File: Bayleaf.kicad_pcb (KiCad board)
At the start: 2 copper layers, 137 x 94 mm, 71 parts, among them J2 Conn_01x02_Socket, SW1 SW_SPDT, U1 Nice_Nano_V2

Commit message: images
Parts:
- moved H2 1.00 mm to (111.0, 3.00)
- moved H3 1.00 mm to (135.0, 3.00)
- moved H5 1.00 mm to (111.0, 91.0)
- moved H6 1.00 mm to (135.0, 91.0)
- moved H7 1.00 mm to (111.0, 47.0)
- moved J2 1.00 mm to (116.0, 86.0)
- moved U1 1.00 mm to (123.0, 17.8)
- moved SW1 0.97 mm to (123.0, 91.9)
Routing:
- net col-4L: track 130.8 -> 135.9 mm
- net col-5L: track 103.9 -> 106.7 mm
- net col-2L: track 166.6 -> 167.9 mm
- net col-1L: track 183.0 -> 184.3 mm
- net col-3L: track 171.5 -> 170.3 mm
- net row-4L: track 171.2 -> 172.3 mm
- net col-0L: track 234.6 -> 235.6 mm
- net row-3L: track 185.6 -> 186.2 mm
- net row-2L: track 202.1 -> 202.6 mm
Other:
- board size 137 x 94 mm -> 138 x 94 mm

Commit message: move sw
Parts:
- moved U1 0.91 mm to (123.0, 18.7)
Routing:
- net col-5L: track 106.7 -> 108.3 mm
- net row-4L: track 172.3 -> 171.3 mm
- net row-3L: track 186.2 -> 185.3 mm
- net RESET: track 77.6 -> 76.7 mm
- net RAW: track 94.8 -> 93.8 mm
- net row-2L: track 202.6 -> 201.8 mm
- net row-1L: track 223.4 -> 222.7 mm
- net col-0L: track 235.6 -> 236.1 mm
- net row-0L: track 240.9 -> 240.4 mm

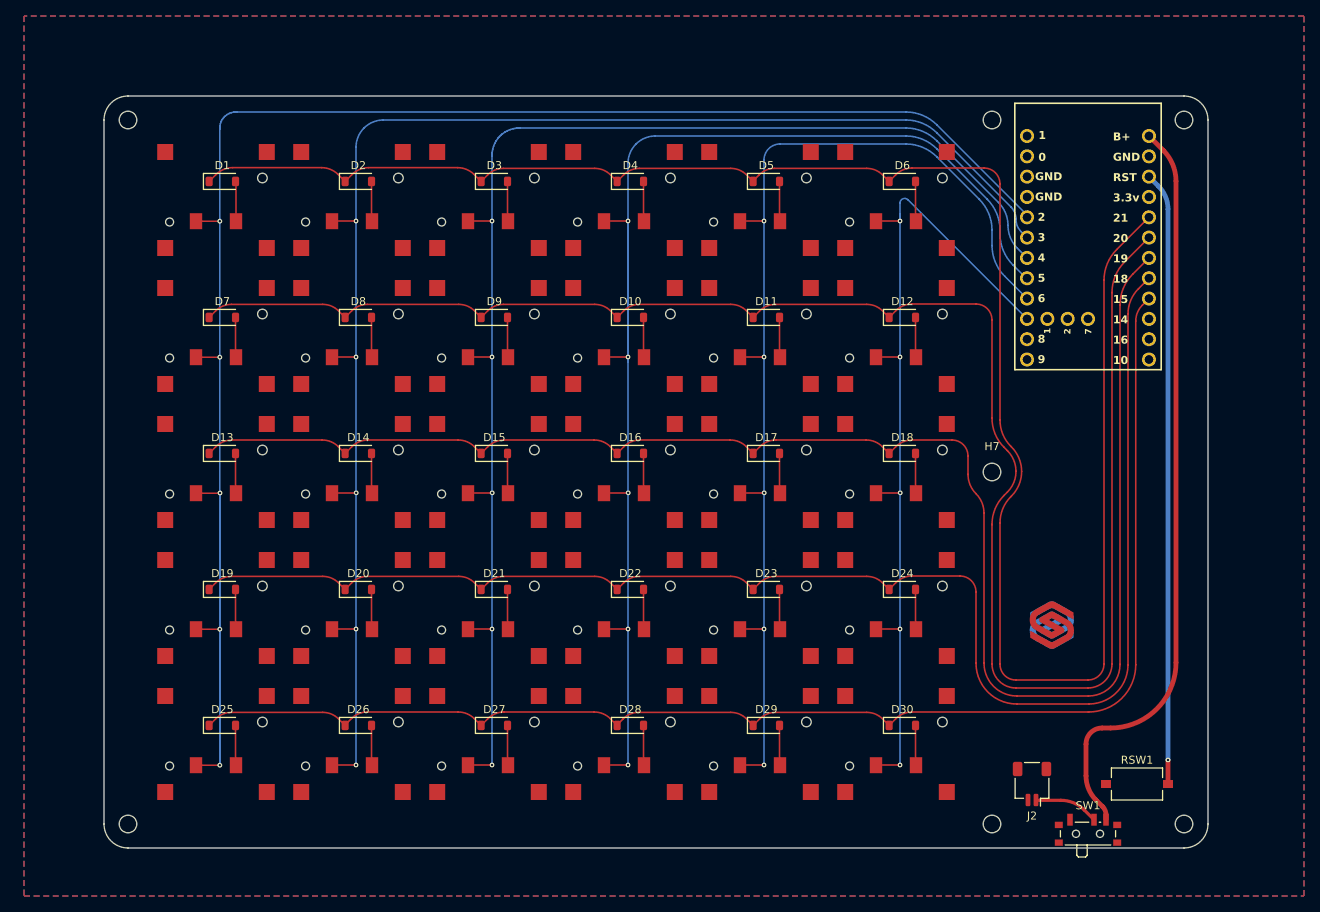
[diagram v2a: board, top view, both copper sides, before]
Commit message: Move components to fit under slope
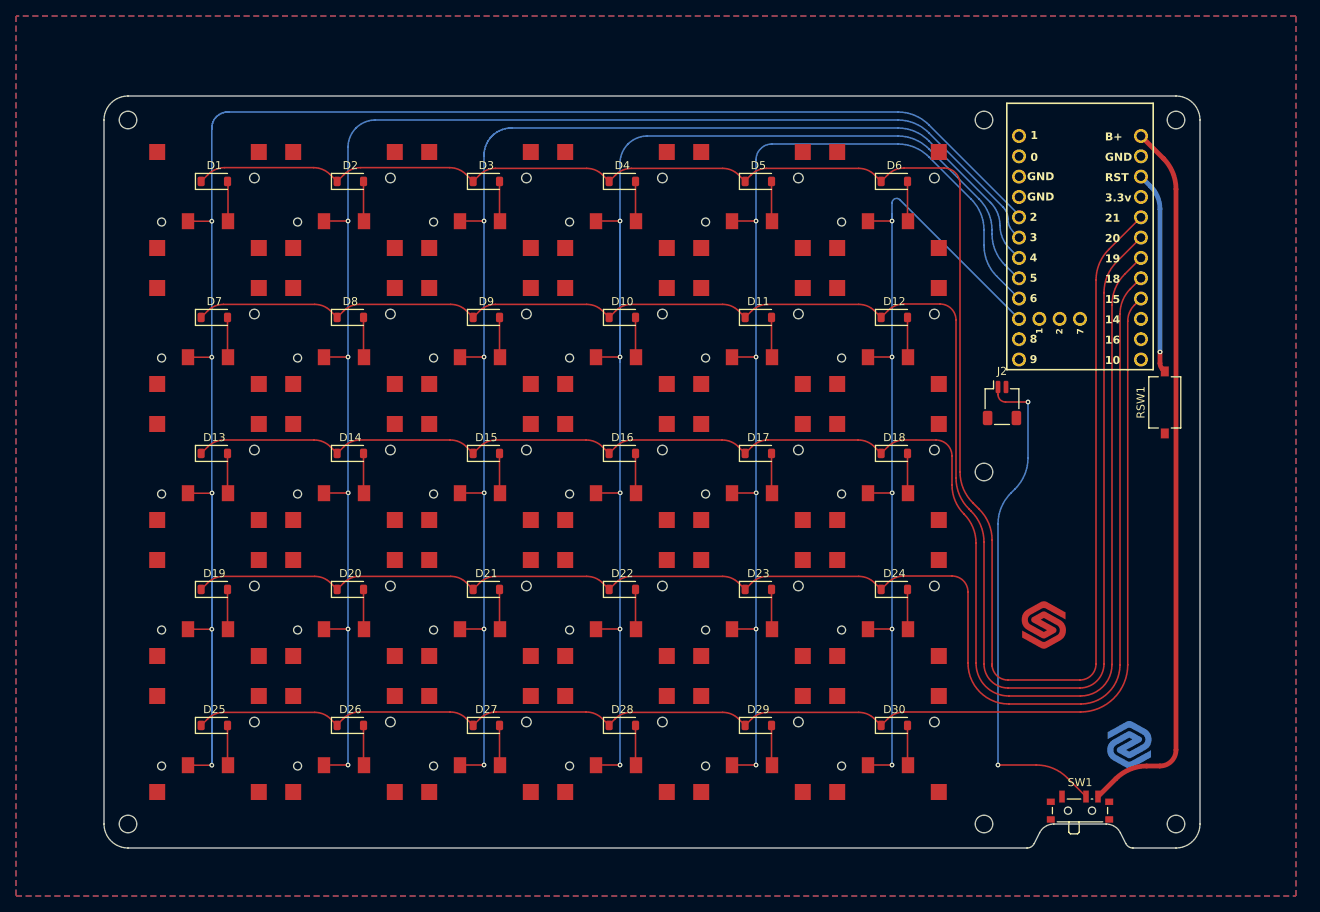
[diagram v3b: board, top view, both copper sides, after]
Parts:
- moved RSW1 47.8 mm to (132.6, 38.3), turned to 90 degrees
- moved J2 47.8 mm to (112.2, 38.4), turned to 0 degrees
- moved SW1 3.06 mm to (122.0, 89.0)
- moved D1 1.00 mm to (13.8, 10.7)
- moved D10 1.00 mm to (64.8, 27.7)
- moved D11 1.00 mm to (81.8, 27.7)
- moved D12 1.00 mm to (98.8, 27.7)
- moved D13 1.00 mm to (13.8, 44.7)
- moved D14 1.00 mm to (30.8, 44.7)
- moved D15 1.00 mm to (47.8, 44.7)
- moved D16 1.00 mm to (64.8, 44.7)
- moved D17 1.00 mm to (81.8, 44.7)
- moved D18 1.00 mm to (98.8, 44.7)
- moved D19 1.00 mm to (13.8, 61.7)
- moved D2 1.00 mm to (30.8, 10.7)
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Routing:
- net +BATT: track 8.07 -> 64.0 mm, vias 0 -> 2
- net RESET: track 76.7 -> 25.3 mm
- net row-1L: track 222.7 -> 218.5 mm
- net row-0L: track 240.4 -> 236.4 mm
- net RAW: track 93.8 -> 90.4 mm
- net row-2L: track 201.8 -> 201.0 mm
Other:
- board size 138 x 94 mm -> 137 x 94 mm

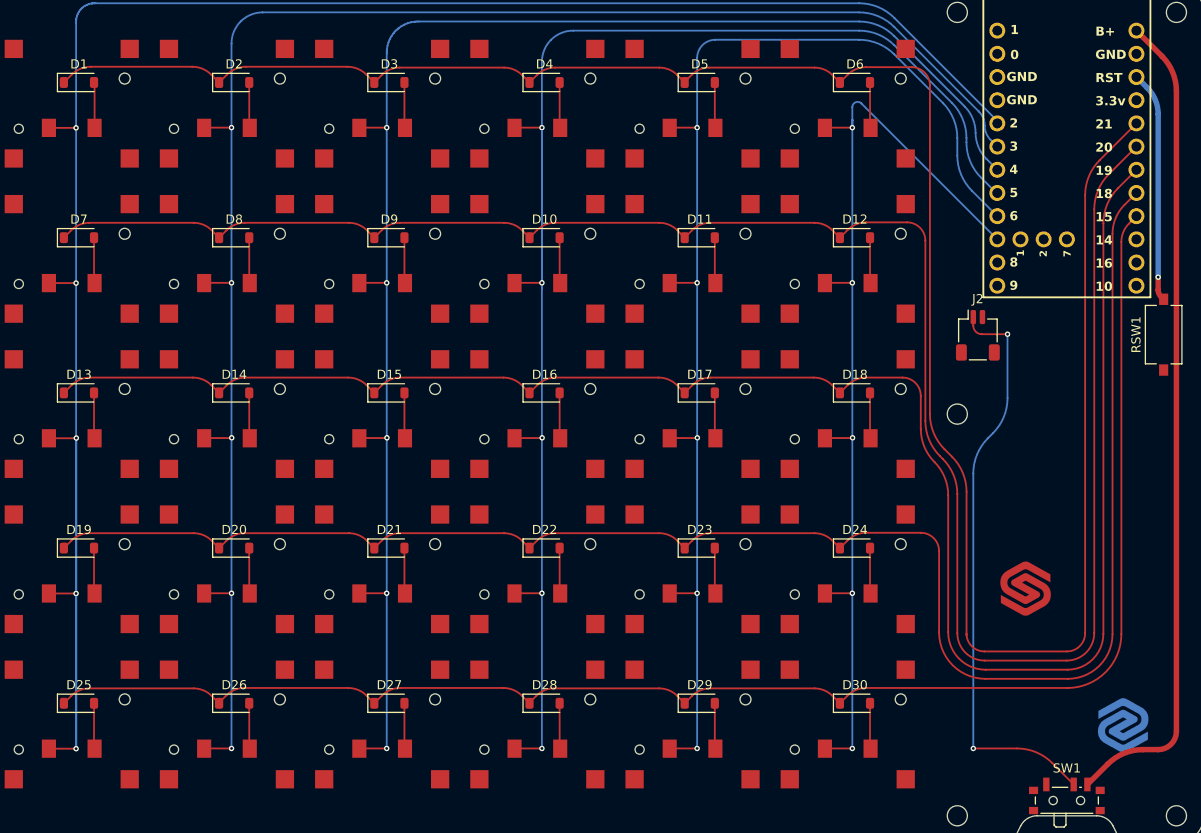
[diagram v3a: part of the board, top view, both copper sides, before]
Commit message: renamed schematic refs
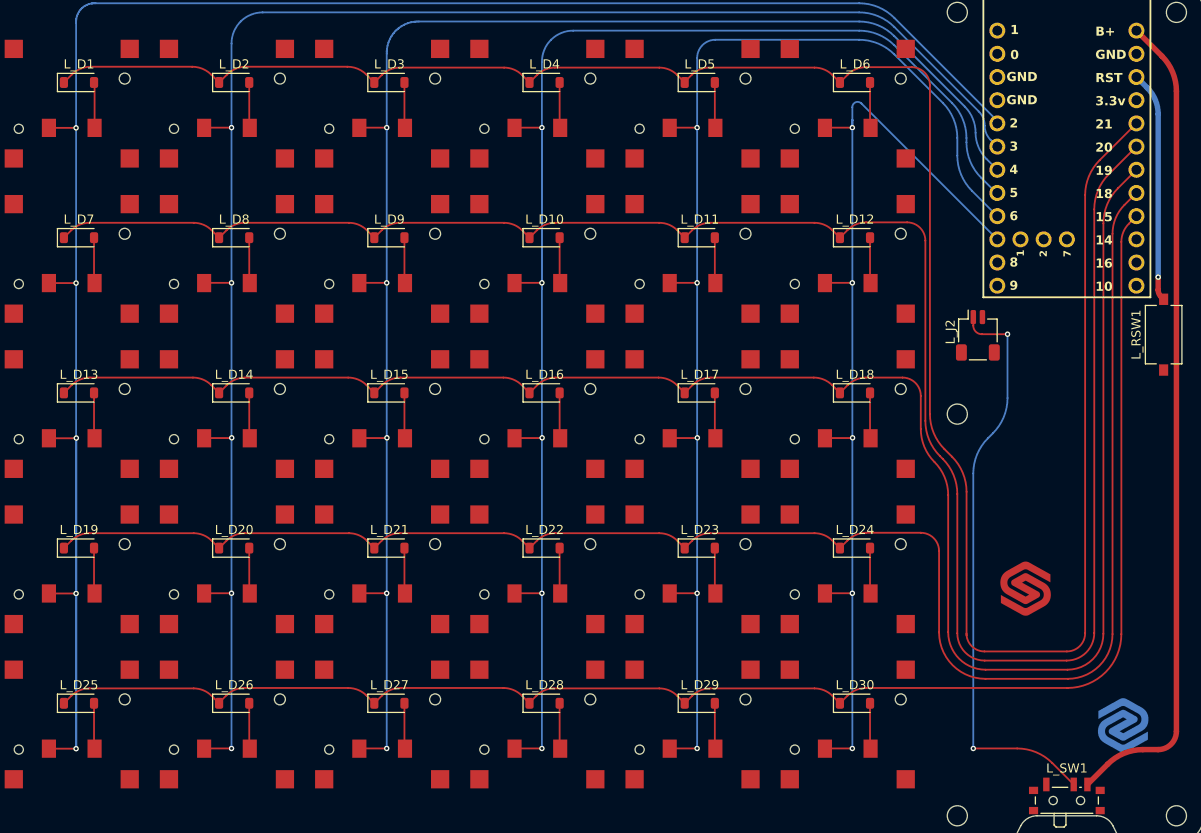
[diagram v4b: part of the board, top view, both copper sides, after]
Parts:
- removed H1, H2, H3, H4, H5, H6, H7: MountingHole, MountingHole:MountingHole_2.2mm_M2
- added L_H1: MountingHole, MountingHole:MountingHole_2.2mm_M2, F.Cu at (3.00, 3.00)
- added L_H2: MountingHole, MountingHole:MountingHole_2.2mm_M2, F.Cu at (110.0, 3.00)
- added L_H3: MountingHole, MountingHole:MountingHole_2.2mm_M2, F.Cu at (134.0, 3.00)
- added L_H4: MountingHole, MountingHole:MountingHole_2.2mm_M2, F.Cu at (3.00, 91.0)
- added L_H5: MountingHole, MountingHole:MountingHole_2.2mm_M2, F.Cu at (110.0, 91.0)
- added L_H6: MountingHole, MountingHole:MountingHole_2.2mm_M2, F.Cu at (134.0, 91.0)
- added L_H7: MountingHole, MountingHole:MountingHole_2.2mm_M2, F.Cu at (110.0, 47.0)
- L_U1: renamed from U1; value Nice_Nano_V2 -> N!N_V2
- renumbered D1 to L_D1, D10 to L_D10, D11 to L_D11, D12 to L_D12, D13 to L_D13, D14 to L_D14, D15 to L_D15, D16 to L_D16, D17 to L_D17, D18 to L_D18, D19 to L_D19, D2 to L_D2, D20 to L_D20, D21 to L_D21, D22 to L_D22, D23 to L_D23, D24 to L_D24, D25 to L_D25, D26 to L_D26, D27 to L_D27, D28 to L_D28, D29 to L_D29, D3 to L_D3, D30 to L_D30, D4 to L_D4, D5 to L_D5, D6 to L_D6, D7 to L_D7, D8 to L_D8, D9 to L_D9, J2 to L_J2, RSW1 to L_RSW1, S1 to L_S1, S10 to L_S10, S11 to L_S11, S12 to L_S12, S13 to L_S13, S14 to L_S14, S15 to L_S15, S16 to L_S16, S17 to L_S17, S18 to L_S18, S19 to L_S19, S2 to L_S2, S20 to L_S20, S21 to L_S21, S22 to L_S22, S23 to L_S23, S24 to L_S24, S25 to L_S25, S26 to L_S26, S27 to L_S27, S28 to L_S28, S29 to L_S29, S3 to L_S3, S30 to L_S30, S4 to L_S4, S5 to L_S5, S6 to L_S6, S7 to L_S7, S8 to L_S8, S9 to L_S9, SW1 to L_SW1

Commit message: ref checkpoint
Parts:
- added R_D1: 1N4148W, Diode_SMD:D_SOD-123, F.Cu at (173.7, 10.8)
- added R_D10: 1N4148W, Diode_SMD:D_SOD-123, F.Cu at (224.7, 27.8)
- added R_D11: 1N4148W, Diode_SMD:D_SOD-123, F.Cu at (241.7, 27.8)
- added R_D12: 1N4148W, Diode_SMD:D_SOD-123, F.Cu at (258.7, 27.8)
- added R_D13: 1N4148W, Diode_SMD:D_SOD-123, F.Cu at (173.7, 44.8)
- added R_D14: 1N4148W, Diode_SMD:D_SOD-123, F.Cu at (190.7, 44.8)
- added R_D15: 1N4148W, Diode_SMD:D_SOD-123, F.Cu at (207.7, 44.8)
- added R_D16: 1N4148W, Diode_SMD:D_SOD-123, F.Cu at (224.7, 44.8)
- added R_D17: 1N4148W, Diode_SMD:D_SOD-123, F.Cu at (241.7, 44.8)
- added R_D18: 1N4148W, Diode_SMD:D_SOD-123, F.Cu at (258.7, 44.8)
- added R_D19: 1N4148W, Diode_SMD:D_SOD-123, F.Cu at (173.7, 61.8)
- added R_D2: 1N4148W, Diode_SMD:D_SOD-123, F.Cu at (190.7, 10.8)
- added R_D20: 1N4148W, Diode_SMD:D_SOD-123, F.Cu at (190.7, 61.8)
- added R_D21: 1N4148W, Diode_SMD:D_SOD-123, F.Cu at (207.7, 61.8)
- added R_D22: 1N4148W, Diode_SMD:D_SOD-123, F.Cu at (224.7, 61.8)
- added R_D23: 1N4148W, Diode_SMD:D_SOD-123, F.Cu at (241.7, 61.8)
- added R_D24: 1N4148W, Diode_SMD:D_SOD-123, F.Cu at (258.7, 61.8)
- added R_D25: 1N4148W, Diode_SMD:D_SOD-123, F.Cu at (173.7, 78.8)
- added R_D26: 1N4148W, Diode_SMD:D_SOD-123, F.Cu at (190.7, 78.8)
- added R_D27: 1N4148W, Diode_SMD:D_SOD-123, F.Cu at (207.7, 78.8)
- added R_D28: 1N4148W, Diode_SMD:D_SOD-123, F.Cu at (224.7, 78.8)
- added R_D29: 1N4148W, Diode_SMD:D_SOD-123, F.Cu at (241.7, 78.8)
- added R_D3: 1N4148W, Diode_SMD:D_SOD-123, F.Cu at (207.7, 10.8)
- added R_D30: 1N4148W, Diode_SMD:D_SOD-123, F.Cu at (258.7, 78.8)
- added R_D4: 1N4148W, Diode_SMD:D_SOD-123, F.Cu at (224.7, 10.8)
- added R_D5: 1N4148W, Diode_SMD:D_SOD-123, F.Cu at (241.7, 10.8)
- added R_D6: 1N4148W, Diode_SMD:D_SOD-123, F.Cu at (258.7, 10.8)
- added R_D7: 1N4148W, Diode_SMD:D_SOD-123, F.Cu at (173.7, 27.8)
- added R_D8: 1N4148W, Diode_SMD:D_SOD-123, F.Cu at (190.7, 27.8)
- added R_D9: 1N4148W, Diode_SMD:D_SOD-123, F.Cu at (207.7, 27.8)
- added R_H1: MountingHole, MountingHole:MountingHole_2.2mm_M2, F.Cu at (163.0, 3.15)
- added R_H2: MountingHole, MountingHole:MountingHole_2.2mm_M2, F.Cu at (270.0, 3.15)
- added R_H3: MountingHole, MountingHole:MountingHole_2.2mm_M2, F.Cu at (294.0, 3.15)
- added R_H4: MountingHole, MountingHole:MountingHole_2.2mm_M2, F.Cu at (270.0, 47.2)
- added R_H5: MountingHole, MountingHole:MountingHole_2.2mm_M2, F.Cu at (163.0, 91.2)
- added R_H6: MountingHole, MountingHole:MountingHole_2.2mm_M2, F.Cu at (270.0, 91.2)
- added R_H7: MountingHole, MountingHole:MountingHole_2.2mm_M2, F.Cu at (294.0, 91.2)
- added R_J1: Conn_01x02_Socket, Connector_JST:JST_SH_SM02B-SRSS-TB_1x02-1MP_P1.00mm_Horizontal, F.Cu at (272.2, 38.5)
- added R_RSW1: SW_RST, Button_Switch_SMD:SW_Tactile_SPST_NO_Straight_CK_PTS636Sx25SMTRLFS, F.Cu at (292.6, 38.5)
- added R_S1: Keyswitch, Bayleaf:CPG1316S01D02_mikeholscher, F.Cu at (173.0, 13.2)
- added R_S10: Keyswitch, Bayleaf:CPG1316S01D02_mikeholscher, F.Cu at (224.0, 30.2)
- added R_S11: Keyswitch, Bayleaf:CPG1316S01D02_mikeholscher, F.Cu at (241.0, 30.2)
- added R_S12: Keyswitch, Bayleaf:CPG1316S01D02_mikeholscher, F.Cu at (258.0, 30.2)
- added R_S13: Keyswitch, Bayleaf:CPG1316S01D02_mikeholscher, F.Cu at (173.0, 47.2)
- added R_S14: Keyswitch, Bayleaf:CPG1316S01D02_mikeholscher, F.Cu at (190.0, 47.2)
- added R_S15: Keyswitch, Bayleaf:CPG1316S01D02_mikeholscher, F.Cu at (207.0, 47.2)
- added R_S16: Keyswitch, Bayleaf:CPG1316S01D02_mikeholscher, F.Cu at (224.0, 47.2)
- added R_S17: Keyswitch, Bayleaf:CPG1316S01D02_mikeholscher, F.Cu at (241.0, 47.2)
- added R_S18: Keyswitch, Bayleaf:CPG1316S01D02_mikeholscher, F.Cu at (258.0, 47.2)
- added R_S19: Keyswitch, Bayleaf:CPG1316S01D02_mikeholscher, F.Cu at (173.0, 64.2)
- added R_S2: Keyswitch, Bayleaf:CPG1316S01D02_mikeholscher, F.Cu at (190.0, 13.2)
- added R_S20: Keyswitch, Bayleaf:CPG1316S01D02_mikeholscher, F.Cu at (190.0, 64.2)
- added R_S21: Keyswitch, Bayleaf:CPG1316S01D02_mikeholscher, F.Cu at (207.0, 64.2)
- added R_S22: Keyswitch, Bayleaf:CPG1316S01D02_mikeholscher, F.Cu at (224.0, 64.2)
- added R_S23: Keyswitch, Bayleaf:CPG1316S01D02_mikeholscher, F.Cu at (241.0, 64.2)
- added R_S24: Keyswitch, Bayleaf:CPG1316S01D02_mikeholscher, F.Cu at (258.0, 64.2)
- added R_S25: Keyswitch, Bayleaf:CPG1316S01D02_mikeholscher, F.Cu at (173.0, 81.2)
- added R_S26: Keyswitch, Bayleaf:CPG1316S01D02_mikeholscher, F.Cu at (190.0, 81.2)
- added R_S27: Keyswitch, Bayleaf:CPG1316S01D02_mikeholscher, F.Cu at (207.0, 81.2)
- added R_S28: Keyswitch, Bayleaf:CPG1316S01D02_mikeholscher, F.Cu at (224.0, 81.2)
- added R_S29: Keyswitch, Bayleaf:CPG1316S01D02_mikeholscher, F.Cu at (241.0, 81.2)
- added R_S3: Keyswitch, Bayleaf:CPG1316S01D02_mikeholscher, F.Cu at (207.0, 13.2)
- added R_S30: Keyswitch, Bayleaf:CPG1316S01D02_mikeholscher, F.Cu at (258.0, 81.2)
- added R_S4: Keyswitch, Bayleaf:CPG1316S01D02_mikeholscher, F.Cu at (224.0, 13.2)
- added R_S5: Keyswitch, Bayleaf:CPG1316S01D02_mikeholscher, F.Cu at (241.0, 13.2)
- added R_S6: Keyswitch, Bayleaf:CPG1316S01D02_mikeholscher, F.Cu at (258.0, 13.2)
- added R_S7: Keyswitch, Bayleaf:CPG1316S01D02_mikeholscher, F.Cu at (173.0, 30.2)
- added R_S8: Keyswitch, Bayleaf:CPG1316S01D02_mikeholscher, F.Cu at (190.0, 30.2)
- added R_S9: Keyswitch, Bayleaf:CPG1316S01D02_mikeholscher, F.Cu at (207.0, 30.2)
- added R_SW1: SW_SPDT, Button_Switch_SMD:SW_SPDT_PCM12, F.Cu at (282.0, 89.2)
- added R_U1: N!N_V2, ScottoKeebs_MCU:Nice_Nano_V2, F.Cu at (282.0, 18.9)
- moved L_U1 0.09 mm to (122.0, 18.8)
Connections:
- net +BATT renamed +BATT_L
- net GND renamed GND_L
- net RAW renamed RAW_L
- net RESET renamed RESET_L
- net VCC renamed VCC_L
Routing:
- net row-0R: track 0.00 -> 236.4 mm
- net col-0R: track 0.00 -> 236.1 mm, vias 0 -> 5
- net row-1R: track 0.00 -> 218.5 mm
- net row-2R: track 0.00 -> 201.0 mm
- net row-3R: track 0.00 -> 185.3 mm
- net col-1R: track 0.00 -> 184.6 mm, vias 0 -> 5
- net row-4R: track 0.00 -> 171.3 mm
- net col-3R: track 0.00 -> 170.1 mm, vias 0 -> 5
- net col-2R: track 0.00 -> 168.0 mm, vias 0 -> 5
- net col-4R: track 0.00 -> 135.4 mm, vias 0 -> 5
- net col-5R: track 0.00 -> 108.3 mm, vias 0 -> 5
- net RAW_R: track 0.00 -> 90.4 mm
- net +BATT: track 0.00 -> 64.0 mm, vias 0 -> 2
- net RESET_R: track 0.00 -> 25.3 mm, vias 0 -> 1
- net Net-(R_D9-A): track 0.00 -> 4.99 mm
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- added copper zone on B.Cu, net GND_R
- added copper zone on F.Cu, net GND_R
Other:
- board size 137 x 94 mm -> 297 x 94.2 mm
